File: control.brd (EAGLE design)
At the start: 186 x 186 mm, 103 parts, among them CN1 40PIN FPC, CN2 MINI B USB, CN3 2X10 HEADER, CN4 2X10 HEADER, SW1 TACT, SW10 TACT, SW11 TACT, SW12 TACT, SW13 TACT, SW14 TACT, SW15 TACT, SW16 TACT, SW2 TACT, SW3 TACT, SW4 TACT, SW5 TACT, SW6 TACT, SW7 TACT, SW8 TACT, SW9 TACT, U1 STM32H743ZI, U2 AS4C8M16SA, U3 TPS61169, U4 USBLC6-2SC6, U5 FT230X, U6 DCDC 3V3

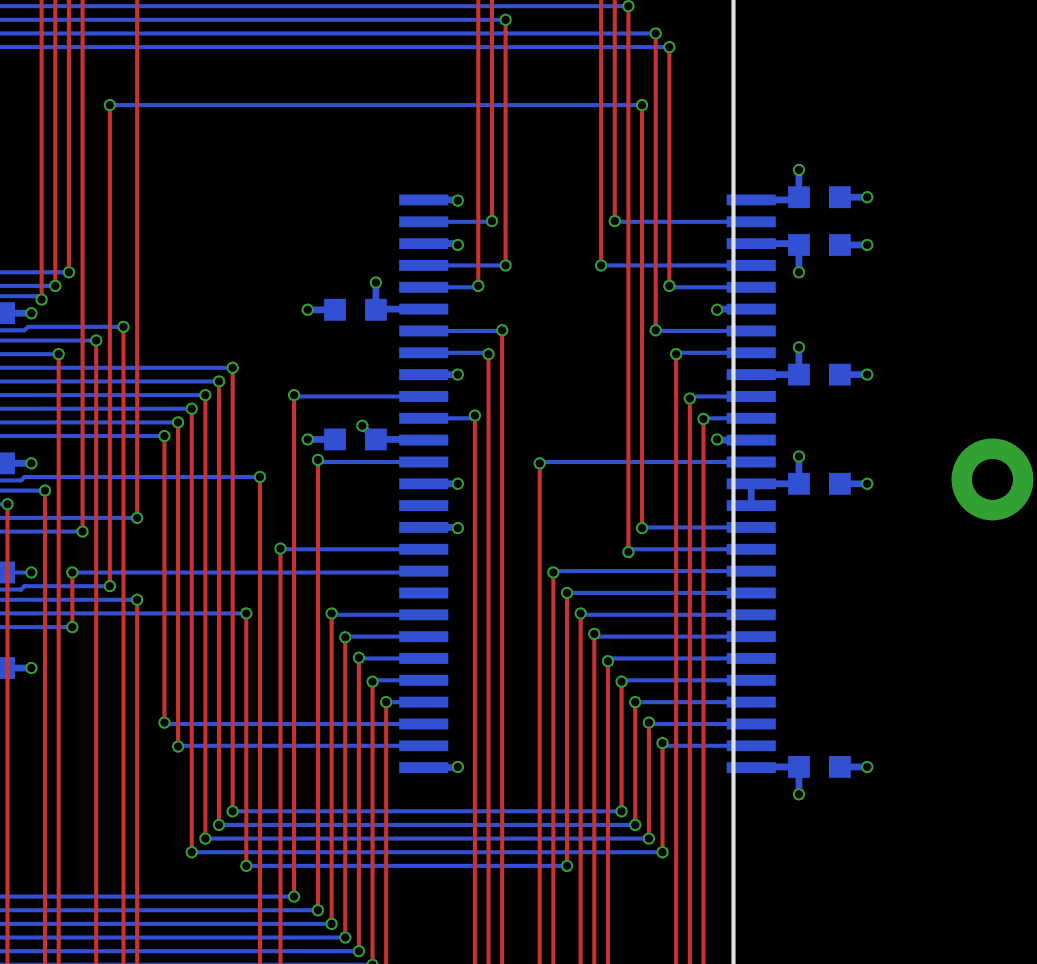
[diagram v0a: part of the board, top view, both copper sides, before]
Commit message: Fixes for stability
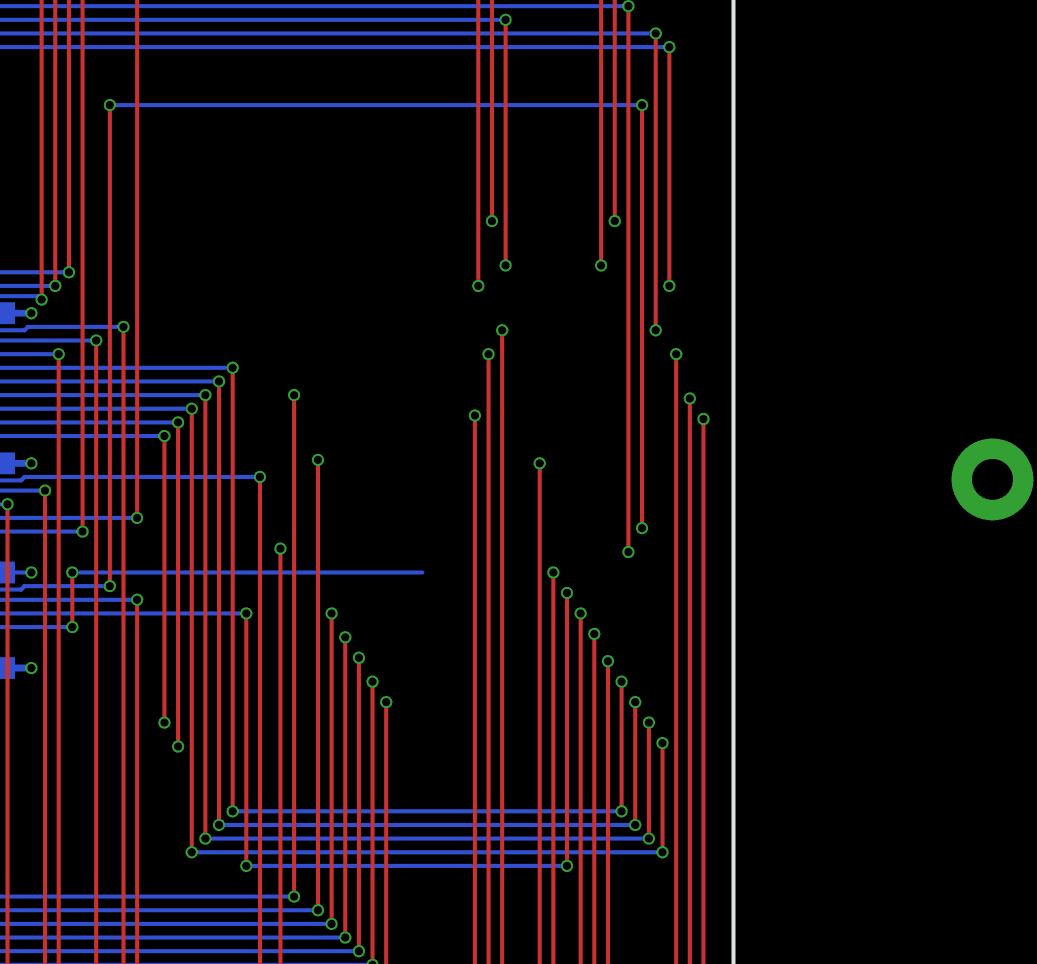
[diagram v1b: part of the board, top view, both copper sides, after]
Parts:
- removed C18, C19, C20, C21, C22, C23, C24: 100nF 16V, CAPACITORS:0603
- removed U2: AS4C8M16SA, ICs:TSOPII_54L_100MIL
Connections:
- net 3V3: now also SW1.3, SW10.3, SW11.3, SW12.3, SW13.3, SW14.3, SW15.3, SW16.3, SW2.3, SW3.3, SW4.3, SW5.3, SW6.3, SW7.3, SW8.3, SW9.3; no longer C18.2, C19.2, C20.2, C21.2, C22.2, C23.2, C24.2, SW1.2, SW10.2, SW11.2, SW12.2, SW13.2, SW14.2, SW15.2, SW16.2, SW2.2, SW3.2, SW4.2, SW5.2, SW6.2, SW7.2, SW8.2, SW9.2, U2.1, U2.14, U2.15, U2.27, U2.3, U2.39, U2.43, U2.49, U2.9
- net GND: no longer C18.1, C19.1, C20.1, C21.1, C22.1, C23.1, C24.1, U2.12, U2.28, U2.41, U2.46, U2.52, U2.54, U2.6
- net N$48: now also SW1.2; no longer SW1.3
- net N$50: now also SW2.2; no longer SW2.3
- net N$52: now also SW3.2; no longer SW3.3
- net N$54: now also SW4.2; no longer SW4.3
- net N$56: now also SW5.2; no longer SW5.3
- net N$58: now also SW6.2; no longer SW6.3
- net N$60: now also SW7.2; no longer SW7.3
- net N$62: now also SW8.2; no longer SW8.3
- net N$64: now also SW9.2; no longer SW9.3
- net N$66: now also SW10.2; no longer SW10.3
- net N$68: now also SW11.2; no longer SW11.3
- net N$70: now also SW12.2; no longer SW12.3
- net N$72: now also SW13.2; no longer SW13.3
- net N$74: now also SW14.2; no longer SW14.3
- net N$76: now also SW15.2; no longer SW15.3
- net N$78: now also SW16.2; no longer SW16.3
- net SDRAM_!CAS: no longer U2.17
- net SDRAM_!CS: no longer U2.19
- net SDRAM_!RAS: no longer U2.18
- net SDRAM_!WE: no longer U2.16
- net SDRAM_A0: no longer U2.23
- net SDRAM_A1: no longer U2.24
- net SDRAM_A10: no longer U2.22
- net SDRAM_A11: no longer U2.35
- net SDRAM_A2: no longer U2.25
- net SDRAM_A3: no longer U2.26
- net SDRAM_A4: no longer U2.29
- net SDRAM_A5: no longer U2.30
- net SDRAM_A6: no longer U2.31
- net SDRAM_A7: no longer U2.32
- net SDRAM_A8: no longer U2.33
- net SDRAM_A9: no longer U2.34
- net SDRAM_BA0: no longer U2.20
- net SDRAM_BA1: no longer U2.21
- net SDRAM_CKE: no longer U2.37
- net SDRAM_CLK: no longer U2.38
- net SDRAM_D0: no longer U2.2
- net SDRAM_D1: no longer U2.4
- net SDRAM_D10: no longer U2.45
- net SDRAM_D11: no longer U2.47
- net SDRAM_D12: no longer U2.48
- net SDRAM_D13: no longer U2.50
- net SDRAM_D14: no longer U2.51
- net SDRAM_D15: no longer U2.53
- net SDRAM_D2: no longer U2.5
- net SDRAM_D3: no longer U2.7
- net SDRAM_D4: no longer U2.8
- net SDRAM_D5: no longer U2.10
- net SDRAM_D6: no longer U2.11
- net SDRAM_D7: no longer U2.13
- net SDRAM_D8: no longer U2.42
- net SDRAM_D9: no longer U2.44
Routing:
- net 3V3: track 67.4 -> 46.3 mm, vias 28 -> 20
- net GND: track 94.3 -> 78.5 mm, vias 93 -> 79
- net SDRAM_A5: track 28.9 -> 19.4 mm
- net SDRAM_A4: track 30.3 -> 21.3 mm
- net SDRAM_D7: track 81.9 -> 74.2 mm
- net SDRAM_!RAS: track 69.9 -> 62.7 mm
- net SDRAM_!CS: track 49.6 -> 42.9 mm
- net SDRAM_BA0: track 99.9 -> 93.7 mm
- net SDRAM_BA1: track 97.7 -> 92.0 mm
- net SDRAM_D1: track 107.6 -> 102.1 mm
- net SDRAM_CLK: track 99.3 -> 94.0 mm
- net SDRAM_A10: track 67.9 -> 62.8 mm
- net SDRAM_D0: track 106.6 -> 101.6 mm
- net SDRAM_D10: track 60.4 -> 55.7 mm
- net SDRAM_A0: track 51.4 -> 46.7 mm
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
